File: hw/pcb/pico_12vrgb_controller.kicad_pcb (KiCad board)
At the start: 2 copper layers, 18 parts, among them J1 Conn_01x04_RGB, J2 Conn_01x04_RGB, J3 Conn_01x04_RGB, J4 Conn_01x04_RGB, J5 Conn_01x03_Male, Q1 DMG2302U, Q10 DMG2302U, Q11 DMG2302U, Q12 DMG2302U, Q2 DMG2302U, Q3 DMG2302U, Q4 DMG2302U, Q5 DMG2302U, Q6 DMG2302U, Q7 DMG2302U, Q8 DMG2302U, Q9 DMG2302U, U1 Raspberry_Pi_Pico

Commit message: Add custom model and footprint for SATA connector
I might need to change this, because the ModDIY listing shows two
different connectors in the pictures, but only has one data sheet
picture. Hopefully both connectors work with the same footprint.
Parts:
- added J6: Conn_01x03_Male, Connector_PinHeader_2.54mm:PinHeader_1x03_P2.54mm_Vertical, F.Cu at (85.1, 91.4)
- added J7: Sata_15pin_Power, pico_12vrgb_controller:ModDIY_SATA_15pin_RightAngle_Header, F.Cu at (162.6, 76.2)
- moved J5 2.59 mm to (73.1, 91.4)
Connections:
- net Net-(U1-Pad39) renamed VBUS
- U1 pad 41: unconnected-(U1-Pad41) -> /SWCLK
- U1 pad 43: unconnected-(U1-Pad43) -> /SWDIO

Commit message: Add ADC reference to schematic
Planning to use the internal temperature sensor and given the small
voltages involved, adding a reference sounds like a good idea.

Also changes the UART header to be 4 pins, which seems more conventional
even though the power pin will be disconnected.
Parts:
- added U2: LM4040C30FTA, Package_TO_SOT_SMD:SOT-23, F.Cu at (86.4, 61.0)
- J5: value Conn_01x03_Male -> Conn_01x04_Male; footprint Connector_PinHeader_2.54mm:PinHeader_1x03_P2.54mm_Vertical -> Connector_PinHeader_2.54mm:PinHeader_1x04_P2.54mm_Vertical
- moved J6 3.81 mm to (88.9, 91.4)
- moved J5 0.53 mm to (73.7, 91.4)
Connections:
- net VBUS renamed Net-(U1-Pad39)
- J5 pad 2: /UART_TX -> /UART_RX
- J5 pad 3: /UART_RX -> /UART_TX
- U1 pad 35: unconnected-(U1-Pad35) -> Net-(U1-Pad35)

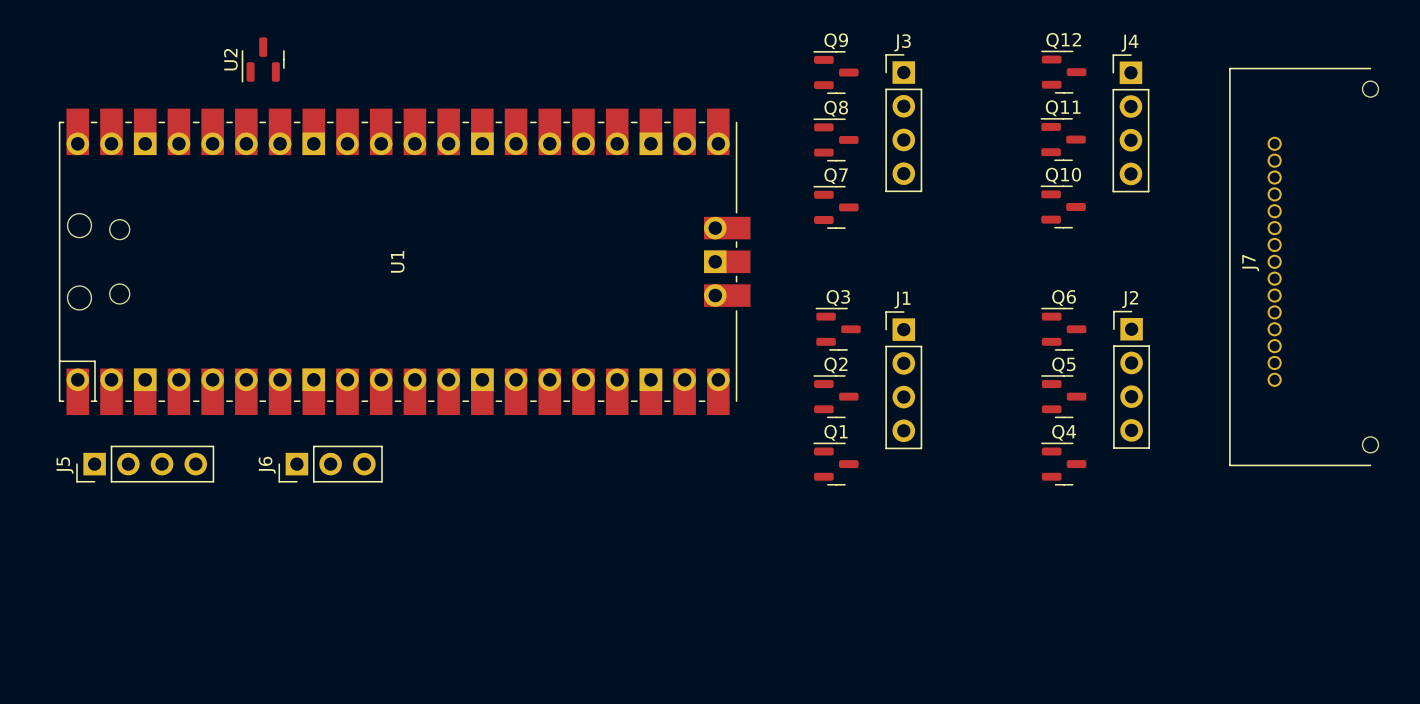
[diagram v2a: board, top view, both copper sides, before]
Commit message: Add PCB board edge and group plane
Also arrange components in one layout that might work, configure the
board properties for OSH Park, and fix alignment and pad sizes in the
SATA connector footprint.
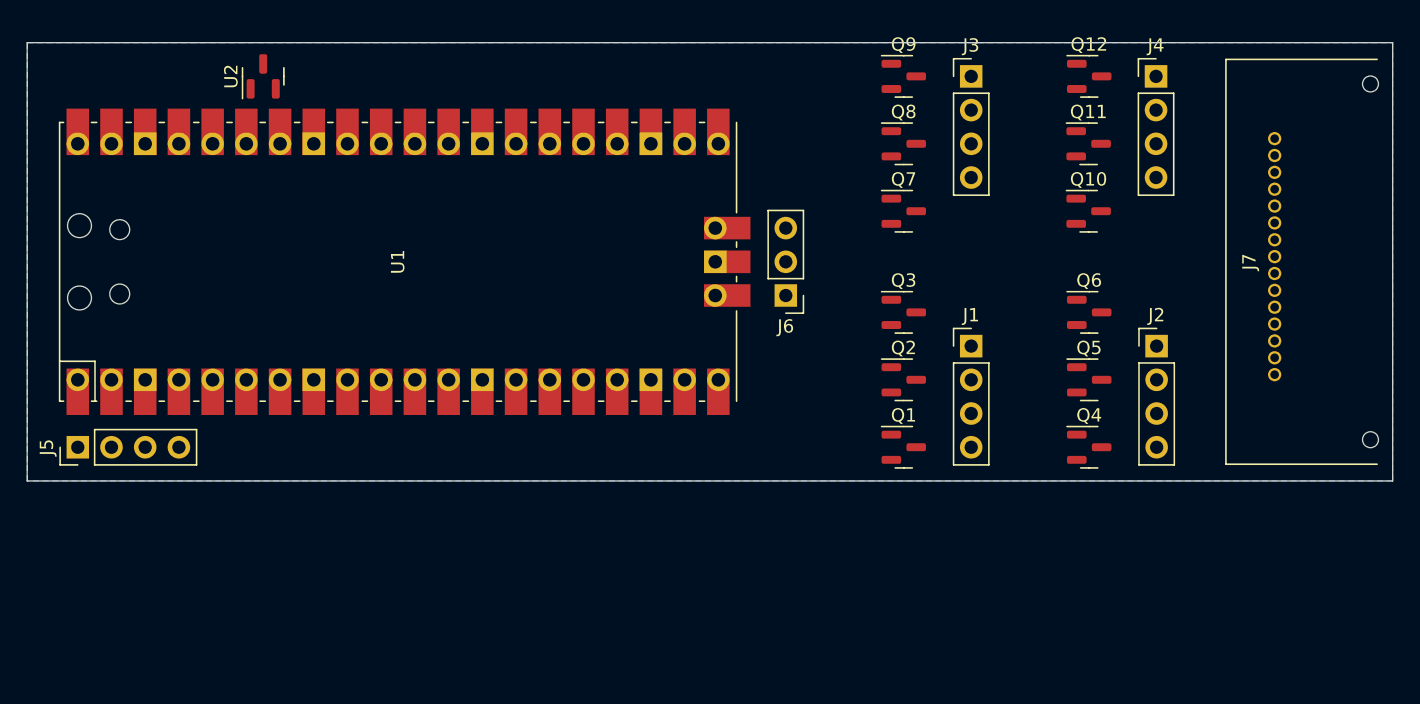
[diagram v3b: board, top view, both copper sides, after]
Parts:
- moved J6 39.0 mm to (125.7, 78.7), turned to 180 degrees
- moved Q1 5.24 mm to (134.6, 90.2)
- moved Q2 5.24 mm to (134.6, 85.1)
- moved J1 5.23 mm to (139.7, 82.5)
- moved Q7 5.09 mm to (134.6, 72.4)
- moved Q8 5.09 mm to (134.6, 67.3)
- moved Q9 5.09 mm to (134.6, 62.2)
- moved J3 5.09 mm to (139.7, 62.2)
- moved Q3 5.08 mm to (134.6, 80.0)
- moved Q4 2.28 mm to (148.6, 90.2)
- moved Q5 2.28 mm to (148.6, 85.1)
- moved Q6 2.28 mm to (148.6, 80.0)
- moved J2 2.28 mm to (153.7, 82.5)
- moved Q12 1.92 mm to (148.6, 62.2)
- moved Q10 1.92 mm to (148.5, 72.4)
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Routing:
- added copper zone on B.Cu, net GND
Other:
- board outline added: 102.9 x 33 mm
- rule pad_to_mask_clearance: 0 -> 0.0508

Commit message: Start routing PCB, change header orientation
The RGB half is mostly complete, although I might shift things around to
save a bit of space. Still need to connect things up to the Pico.
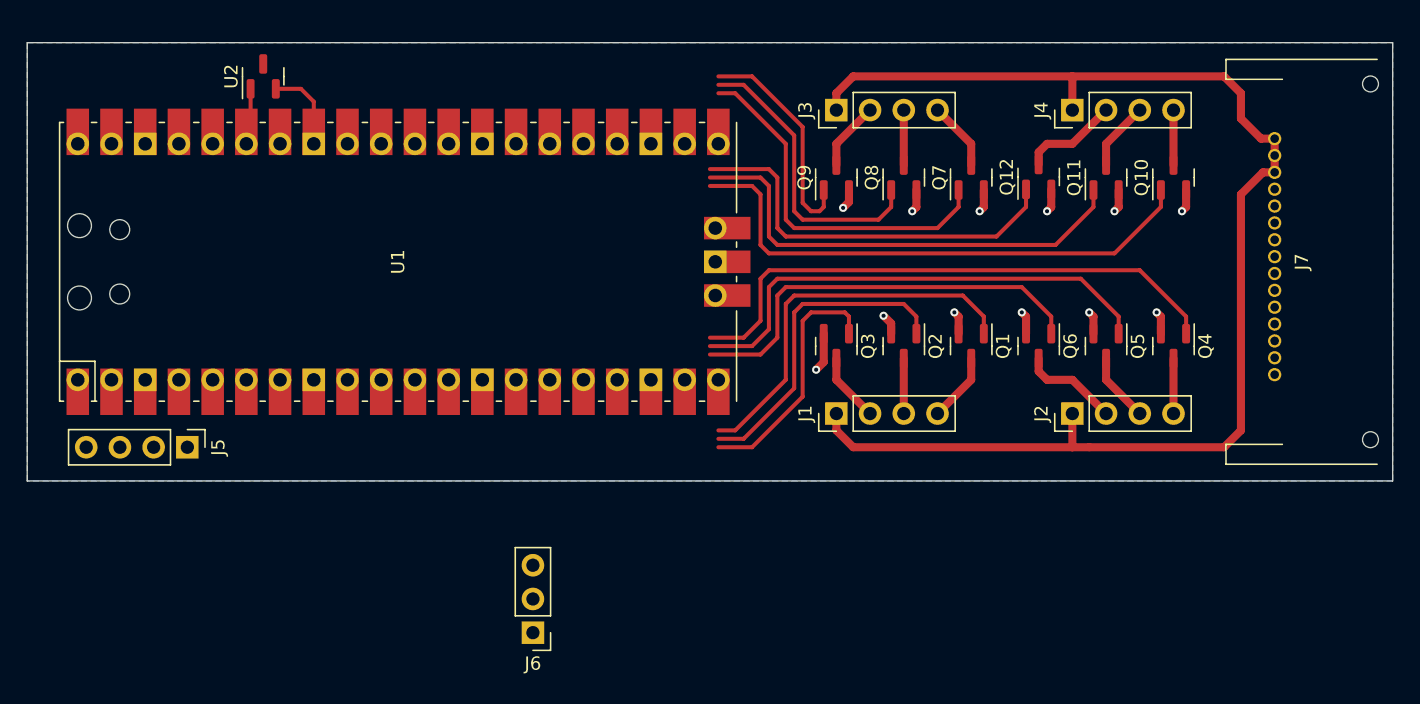
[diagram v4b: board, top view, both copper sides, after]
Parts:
- moved J6 31.8 mm to (106.7, 104.1)
- moved J1 11.4 mm to (129.5, 87.6), turned to 90 degrees
- moved J3 10.5 mm to (129.5, 64.8), turned to 90 degrees
- moved Q4 9.92 mm to (154.9, 82.5), turned to -90 degrees
- moved Q9 9.16 mm to (129.5, 69.8), turned to 90 degrees
- moved Q1 9.16 mm to (139.7, 82.5), turned to -90 degrees
- moved Q12 8.48 mm to (144.8, 69.8), turned to 90 degrees
- moved J5 8.25 mm to (80.6, 90.2), turned to -90 degrees
- moved J2 8.13 mm to (147.3, 87.6), turned to 90 degrees
- moved Q10 6.88 mm to (154.9, 69.8), turned to 90 degrees
- moved J4 6.80 mm to (147.3, 64.8), turned to 90 degrees
- moved Q3 5.68 mm to (129.5, 82.5), turned to -90 degrees
- moved Q7 5.68 mm to (139.7, 69.8), turned to 90 degrees
- moved Q6 4.58 mm to (144.8, 82.5), turned to -90 degrees
- moved Q11 2.86 mm to (149.9, 69.8), turned to 90 degrees
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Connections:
- net Net-(U1-Pad35) renamed /ADC_VREF
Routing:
- net +12V: track 0.00 -> 99.3 mm
- net /L2_PWM_B: track 0.00 -> 42.6 mm
- net /L4_PWM_B: track 0.00 -> 41.0 mm
- net /L2_PWM_R: track 0.00 -> 37.2 mm
- net /L4_PWM_R: track 0.00 -> 35.7 mm
- net /L2_PWM_G: track 0.00 -> 31.9 mm
- net /L4_PWM_G: track 0.00 -> 30.4 mm
- net /L1_PWM_B: track 0.00 -> 29.5 mm
- net GND: track 0.00 -> 28.2 mm, vias 0 -> 12
- net /L3_PWM_B: track 0.00 -> 27.6 mm
- net /L1_PWM_R: track 0.00 -> 24.2 mm
- net /L3_PWM_R: track 0.00 -> 22.3 mm
- net /L1_PWM_G: track 0.00 -> 18.8 mm
- net /L3_PWM_G: track 0.00 -> 16.9 mm
- net /L2_G: track 0.00 -> 7.36 mm
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
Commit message: Finish PCB routing
Reduce the size of the PCB to 5 square inches, although I could probably
get it a bit smaller. Update the RGB header footprints with the correct
pin sizes and nice labels. Finally, reassign PWM pins to enable cleaner
routing.

There's a bunch of DRC failures because I drew a shape over some traces
instead of using a fill zone. I'll have to try this again and see if I
can get the fill zone to do what I want.
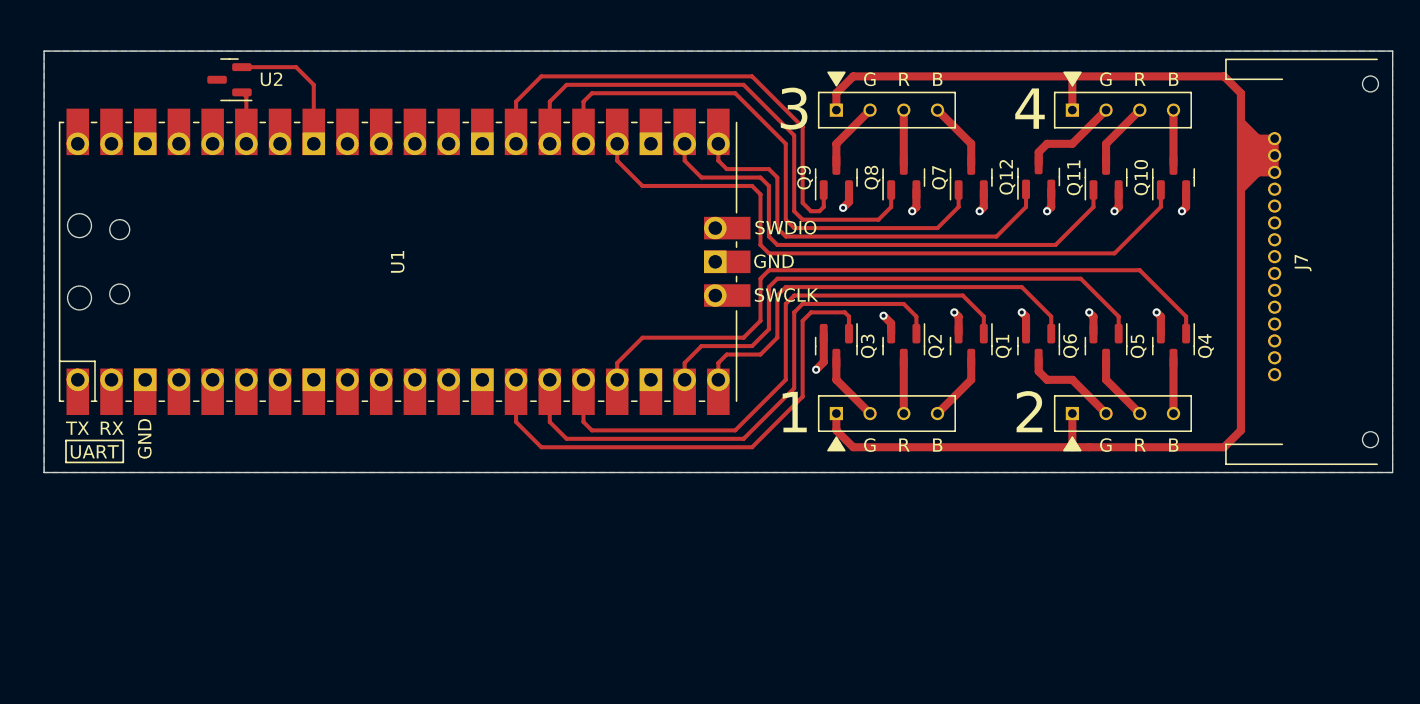
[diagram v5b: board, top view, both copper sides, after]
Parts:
- removed J5: Conn_01x04_Male, Connector_PinHeader_2.54mm:PinHeader_1x04_P2.54mm_Vertical
- removed J6: Conn_01x03_Male, Connector_PinHeader_2.54mm:PinHeader_1x03_P2.54mm_Vertical
- J1, J2: footprint Connector_PinHeader_2.54mm:PinHeader_1x04_P2.54mm_Vertical -> pico_12vrgb_controller:PinHeader_12VGRB_Vertical_LeftText
- J3, J4: footprint Connector_PinHeader_2.54mm:PinHeader_1x04_P2.54mm_Vertical -> pico_12vrgb_controller:PinHeader_12VGRB_Vertical_RightText
- moved U2 2.55 mm to (83.8, 62.5), turned to 180 degrees
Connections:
- U1 pad 10: /L1_PWM_G -> unconnected-(U1-Pad10)
- U1 pad 11: /L1_PWM_B -> unconnected-(U1-Pad11)
- U1 pad 12: /L2_PWM_R -> unconnected-(U1-Pad12)
- U1 pad 14: /L2_PWM_G -> /L1_PWM_G
- U1 pad 15: /L2_PWM_B -> /L1_PWM_R
- U1 pad 16: unconnected-(U1-Pad16) -> /L1_PWM_B
- U1 pad 17: unconnected-(U1-Pad17) -> /L2_PWM_B
- U1 pad 19: unconnected-(U1-Pad19) -> /L2_PWM_R
- U1 pad 20: unconnected-(U1-Pad20) -> /L2_PWM_G
- U1 pad 21: /L3_PWM_R -> /L4_PWM_G
- U1 pad 22: /L3_PWM_G -> /L4_PWM_R
- U1 pad 24: /L3_PWM_B -> /L4_PWM_B
- U1 pad 25: /L4_PWM_R -> /L3_PWM_B
- U1 pad 26: /L4_PWM_G -> /L3_PWM_R
- U1 pad 27: /L4_PWM_B -> /L3_PWM_G
- U1 pad 9: /L1_PWM_R -> unconnected-(U1-Pad9)
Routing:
- net /L3_PWM_G: track 16.9 -> 36.1 mm
- net /L1_PWM_G: track 18.8 -> 38.0 mm
- net /L3_PWM_R: track 22.3 -> 38.7 mm
- net /L1_PWM_R: track 24.2 -> 40.6 mm
- net /L3_PWM_B: track 27.6 -> 41.2 mm
- net /L1_PWM_B: track 29.5 -> 43.1 mm
- net /L2_PWM_B: track 42.6 -> 51.6 mm
- net /L4_PWM_B: track 41.0 -> 50.1 mm
- net +12V: track 99.3 -> 104.8 mm
- net GND: track 28.2 -> 32.1 mm
- net /L2_PWM_R: track 37.2 -> 40.9 mm
- net /L4_PWM_R: track 35.7 -> 39.4 mm
- net /L4_PWM_G: track 30.4 -> 31.3 mm
- net /L2_PWM_G: track 31.9 -> 32.8 mm
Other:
- board size 102.9 x 33 mm -> 101.6 x 31.8 mm
- board text added: "1"
- board text added: "2"
- board text added: "3"
- board text added: "4"
- board text added: "GND"
- board text added: "RX"
- board text added: "SWCLK"
- board text added: "SWDIO"
- board text added: "TX"
- board text added: "UART"

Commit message: Fix 12V fill, minor PCB layout tweaks
Clean up silkscreen, fix remaining DRC errors, expand pads on RGB header
footprints, make the board slightly shorter on the USB end.
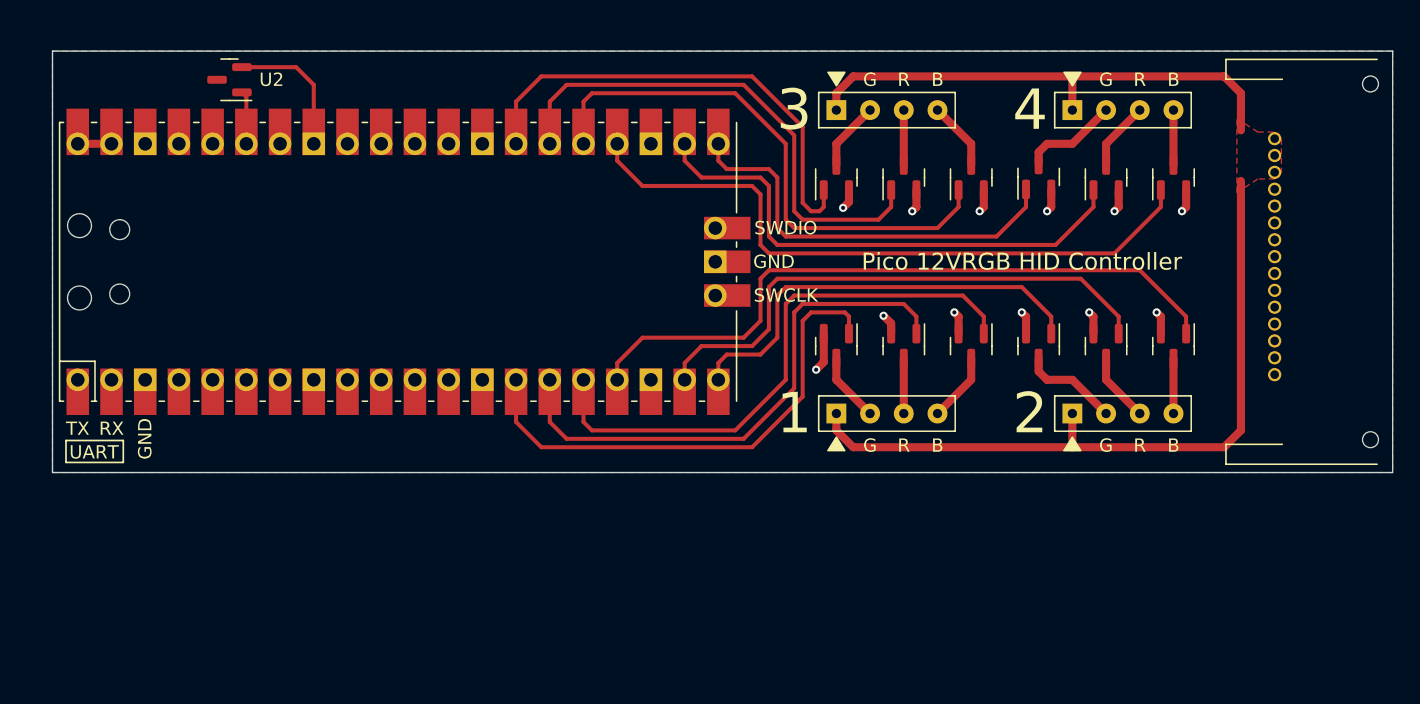
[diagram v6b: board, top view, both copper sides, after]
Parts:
- renumbered J7 to J5
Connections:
- net Net-(U1-Pad39) renamed /VBUS
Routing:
- net +12V: track 104.8 -> 92.3 mm
- net /VBUS: track 0.00 -> 2.54 mm
- added copper zone on F.Cu, net +12V
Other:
- board size 101.6 x 31.8 mm -> 101 x 31.8 mm
- board text added: "Pico 12VRGB HID Controller"

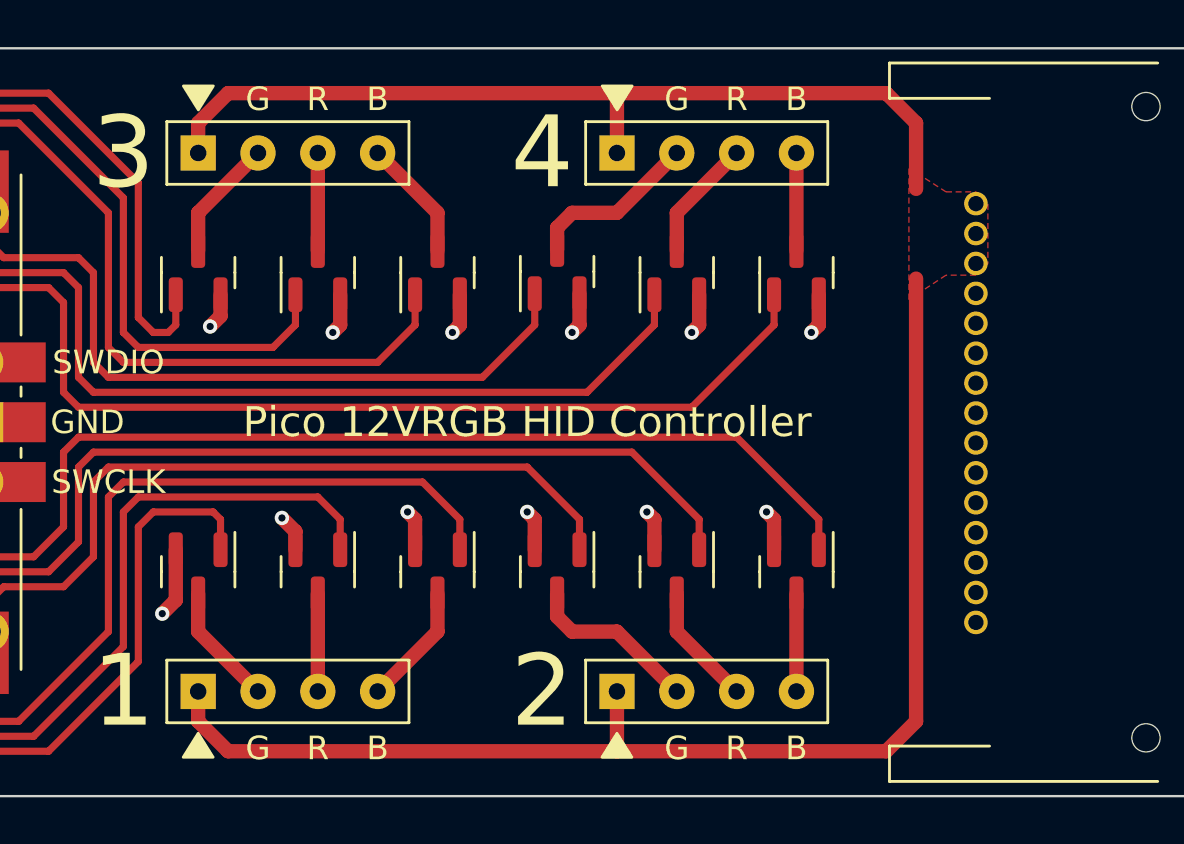
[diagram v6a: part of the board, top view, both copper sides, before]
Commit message: Upgrade to KiCAD 7.0, add mounting hole to PCB
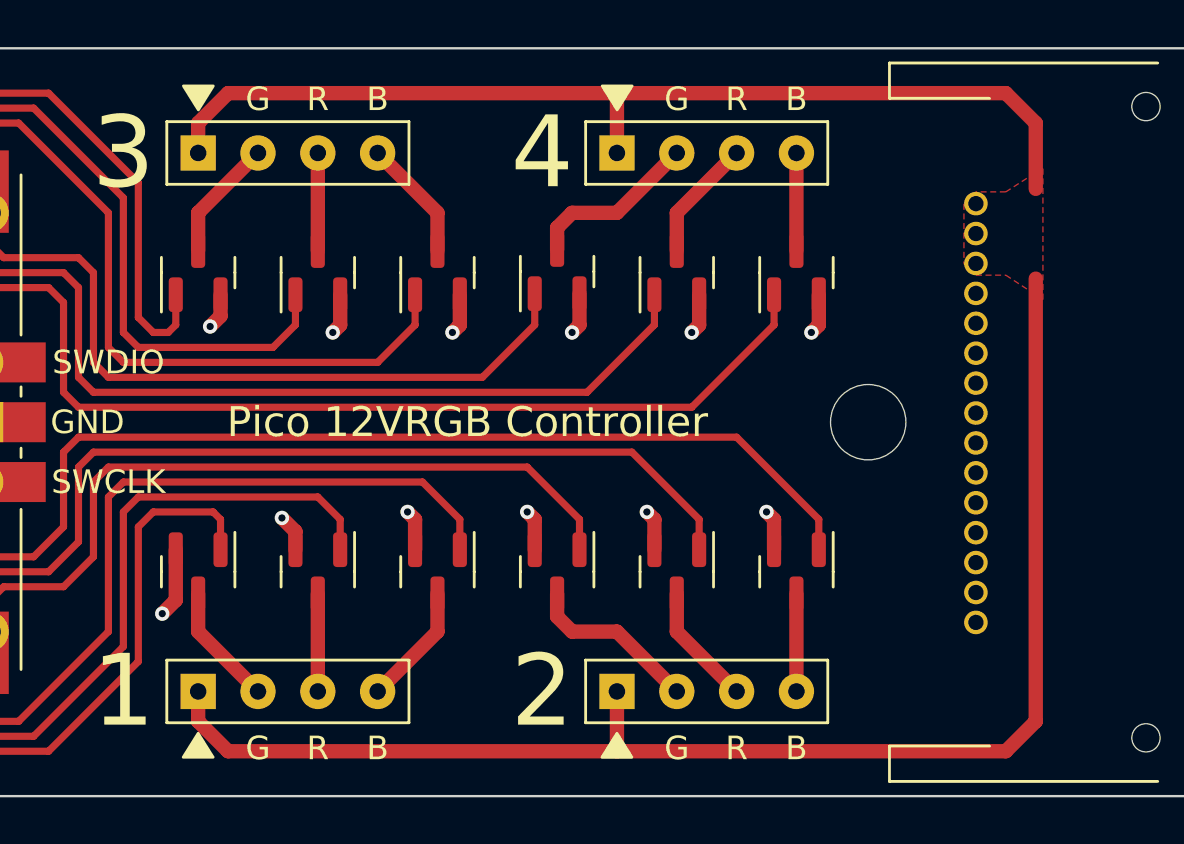
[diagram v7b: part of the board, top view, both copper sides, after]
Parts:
- added REF**: MountingHole_3.2mm_M3, MountingHole:MountingHole_3.2mm_M3, F.Cu at (158.0, 76.2)
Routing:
- net +12V: track 92.3 -> 102.4 mm
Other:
- board text added: "Pico 12VRGB Controller"
- board text removed: "Pico 12VRGB HID Controller"
